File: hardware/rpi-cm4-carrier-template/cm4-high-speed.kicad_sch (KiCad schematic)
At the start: 1 part

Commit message: Added dimensions and updated CM4 component properties to include both receptacle options
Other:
- title: Raspberry Pi Compute Module 4 Shoe Template -> Raspberry Pi Compute Module 4 Carrier Template
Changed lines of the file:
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@@
   (paper "A4")
   (title_block
-    (title "Raspberry Pi Compute Module 4 Shoe Template")
+    (title "Raspberry Pi Compute Module 4 Carrier Template")
     (date "2020-10-31")
     (rev "v01")

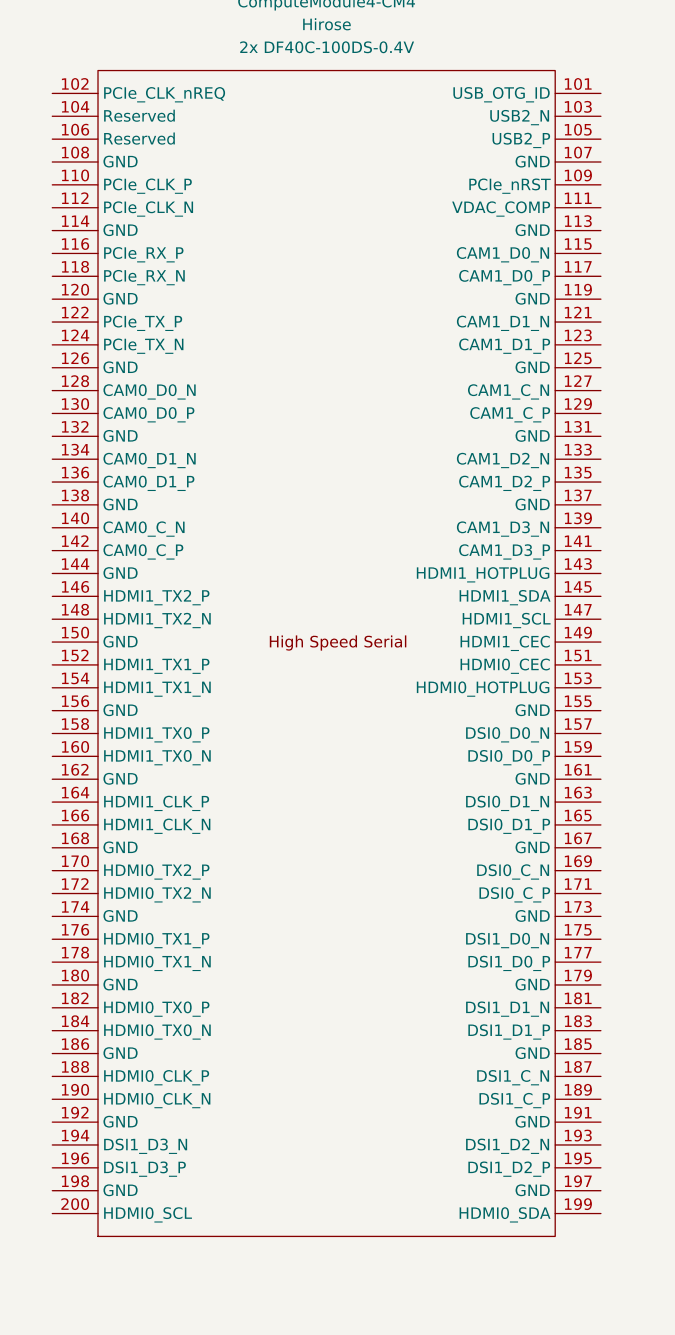
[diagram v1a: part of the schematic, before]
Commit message: Added GND and power lines with labels
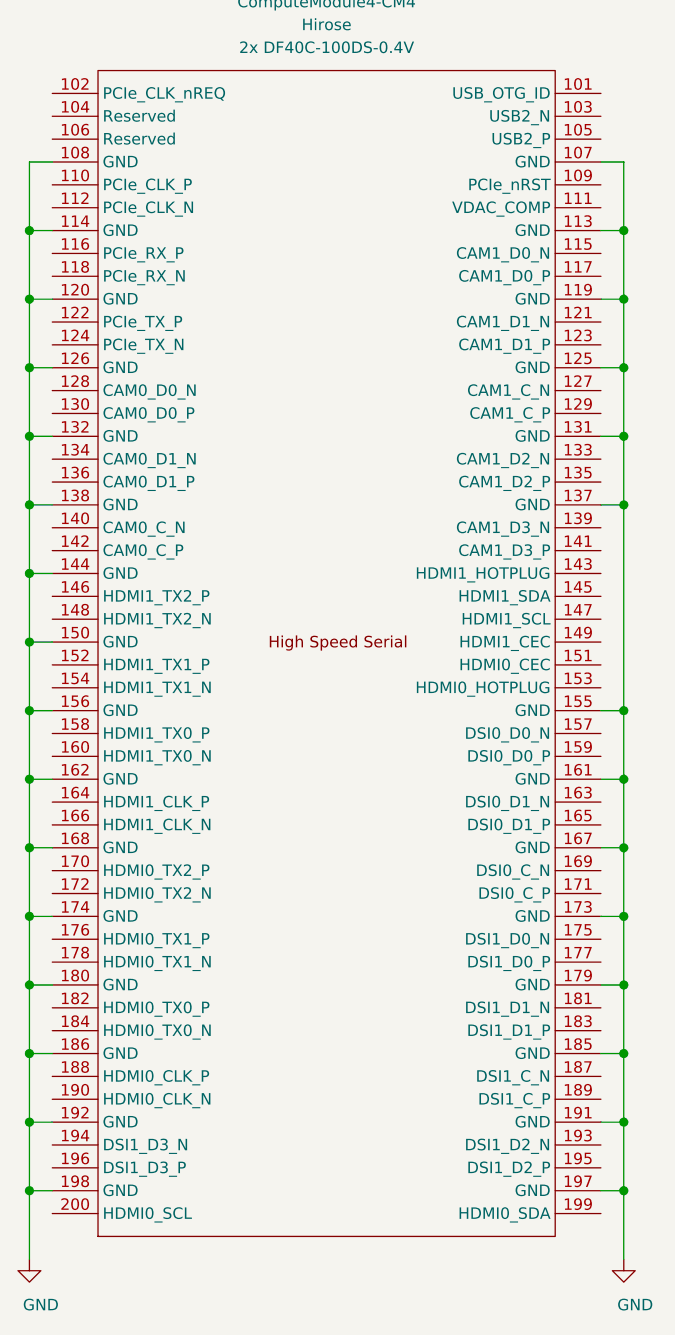
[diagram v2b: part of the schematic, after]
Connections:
- net GND: now reaches Module1.107 (GND)
- net GND: now also Module1.108 (GND), Module1.113 (GND), Module1.114 (GND), Module1.119 (GND), Module1.120 (GND), Module1.125 (GND), Module1.126 (GND), Module1.131 (GND), Module1.132 (GND), Module1.137 (GND), Module1.138 (GND), Module1.144 (GND), Module1.150 (GND), Module1.155 (GND), Module1.156 (GND), Module1.161 (GND), Module1.162 (GND), Module1.167 (GND), Module1.168 (GND), Module1.173 (GND), Module1.174 (GND), Module1.179 (GND), Module1.180 (GND), Module1.185 (GND), Module1.186 (GND), Module1.191 (GND), Module1.192 (GND), Module1.197 (GND), Module1.198 (GND)
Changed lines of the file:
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@@
     (comment 4 "Author: Shawn Hymel")
+  )
+  (junction (at 40.64 60.96) (diameter 1.016) (color 0 0 0 0))
+  (junction (at 40.64 68.58) (diameter 1.016) (color 0 0 0 0))
+  (junction (at 40.64 76.2) (diameter 1.016) (color 0 0 0 0))
+  (junction (at 40.64 83.82) (diameter 1.016) (color 0 0 0 0))
+  (junction (at 40.64 91.44) (diameter 1.016) (color 0 0 0 0))
+  (junction (at 40.64 99.06) (diameter 1.016) (color 0 0 0 0))
+  (junction (at 40.64 106.68) (diameter 1.016) (color 0 0 0 0))
+  (junction (at 40.64 114.3) (diameter 1.016) (color 0 0 0 0))
+  (junction (at 40.64 121.92) (diameter 1.016) (color 0 0 0 0))
+  (junction (at 40.64 129.54) (diameter 1.016) (color 0 0 0 0))
+  (junction (at 40.64 137.16) (diameter 1.016) (color 0 0 0 0))
+  (junction (at 40.64 144.78) (diameter 1.016) (color 0 0 0 0))
+  (junction (at 40.64 152.4) (diameter 1.016) (color 0 0 0 0))
+  (junction (at 40.64 160.02) (diameter 1.016) (color 0 0 0 0))
+  (junction (at 40.64 167.64) (diameter 1.016) (color 0 0 0 0))
+  (junction (at 106.68 60.96) (diameter 1.016) (color 0 0 0 0))
+  (junction (at 106.68 68.58) (diameter 1.016) (color 0 0 0 0))
+  (junction (at 106.68 76.2) (diameter 1.016) (color 0 0 0 0))
+  (junction (at 106.68 83.82) (diameter 1.016) (color 0 0 0 0))
+  (junction (at 106.68 91.44) (diameter 1.016) (color 0 0 0 0))
+  (junction (at 106.68 114.3) (diameter 1.016) (color 0 0 0 0))
+  (junction (at 106.68 121.92) (diameter 1.016) (color 0 0 0 0))
+  (junction (at 106.68 129.54) (diameter 1.016) (color 0 0 0 0))
+  (junction (at 106.68 137.16) (diameter 1.016) (color 0 0 0 0))
+  (junction (at 106.68 144.78) (diameter 1.016) (color 0 0 0 0))
+  (junction (at 106.68 152.4) (diameter 1.016) (color 0 0 0 0))
+  (junction (at 106.68 160.02) (diameter 1.016) (color 0 0 0 0))
+  (junction (at 106.68 167.64) (diameter 1.016) (color 0 0 0 0))
+  (wire (pts (xy 40.64 53.34) (xy 40.64 60.96))
+    (stroke (width 0) (type solid) (color 0 0 0 0))
+  )
+  (wire (pts (xy 40.64 53.34) (xy 43.18 53.34))
+    (stroke (width 0) (type solid) (color 0 0 0 0))
+  )
+  (wire (pts (xy 40.64 60.96) (xy 40.64 68.58))
+    (stroke (width 0) (type solid) (color 0 0 0 0))
+  )
+  (wire (pts (xy 40.64 60.96) (xy 43.18 60.96))
+    (stroke (width 0) (type solid) (color 0 0 0 0))
+  )
+  (wire (pts (xy 40.64 68.58) (xy 40.64 76.2))
+    (stroke (width 0) (type solid) (color 0 0 0 0))
+  )
+  (wire (pts (xy 40.64 68.58) (xy 43.18 68.58))
+    (stroke (width 0) (type solid) (color 0 0 0 0))
+  )
+  (wire (pts (xy 40.64 76.2) (xy 40.64 83.82))
+    (stroke (width 0) (type solid) (color 0 0 0 0))
+  )
+  (wire (pts (xy 40.64 76.2) (xy 43.18 76.2))
+    (stroke (width 0) (type solid) (color 0 0 0 0))
+  )
+  (wire (pts (xy 40.64 83.82) (xy 40.64 91.44))
+    (stroke (width 0) (type solid) (color 0 0 0 0))
+  )
+  (wire (pts (xy 40.64 83.82) (xy 43.18 83.82))
+    (stroke (width 0) (type solid) (color 0 0 0 0))
+  )
+  (wire (pts (xy 40.64 91.44) (xy 40.64 99.06))
+    (stroke (width 0) (type solid) (color 0 0 0 0))
+  )
+  (wire (pts (xy 40.64 91.44) (xy 43.18 91.44))
+    (stroke (width 0) (type solid) (color 0 0 0 0))
+  )
+  (wire (pts (xy 40.64 99.06) (xy 40.64 106.68))
+    (stroke (width 0) (type solid) (color 0 0 0 0))
+  )
+  (wire (pts (xy 40.64 99.06) (xy 43.18 99.06))
+    (stroke (width 0) (type solid) (color 0 0 0 0))
+  )
+  (wire (pts (xy 40.64 106.68) (xy 40.64 114.3))
+    (stroke (width 0) (type solid) (color 0 0 0 0))
+  )
+  (wire (pts (xy 40.64 106.68) (xy 43.18 106.68))
+    (stroke (width 0) (type solid) (color 0 0 0 0))
+  )
+  (wire (pts (xy 40.64 114.3) (xy 40.64 121.92))
+    (stroke (width 0) (type solid) (color 0 0 0 0))
+  )
+  (wire (pts (xy 40.64 114.3) (xy 43.18 114.3))
+    (stroke (width 0) (type solid) (color 0 0 0 0))
+  )
+  (wire (pts (xy 40.64 121.92) (xy 40.64 129.54))
+    (stroke (width 0) (type solid) (color 0 0 0 0))
+  )
+  (wire (pts (xy 40.64 121.92) (xy 43.18 121.92))
+    (stroke (width 0) (type solid) (color 0 0 0 0))
+  )
+  (wire (pts (xy 40.64 129.54) (xy 40.64 137.16))
+    (stroke (width 0) (type solid) (color 0 0 0 0))
+  )
+  (wire (pts (xy 40.64 129.54) (xy 43.18 129.54))
+    (stroke (width 0) (type solid) (color 0 0 0 0))
+  )
+  (wire (pts (xy 40.64 137.16) (xy 40.64 144.78))
+    (stroke (width 0) (type solid) (color 0 0 0 0))
+  )
+  (wire (pts (xy 40.64 137.16) (xy 43.18 137.16))
+    (stroke (width 0) (type solid) (color 0 0 0 0))
+  )
+  (wire (pts (xy 40.64 144.78) (xy 40.64 152.4))
+    (stroke (width 0) (type solid) (color 0 0 0 0))
+  )
+  (wire (pts (xy 40.64 144.78) (xy 43.18 144.78))
+    (stroke (width 0) (type solid) (color 0 0 0 0))
+  )
+  (wire (pts (xy 40.64 152.4) (xy 40.64 160.02))
+    (stroke (width 0) (type solid) (color 0 0 0 0))
+  )
+  (wire (pts (xy 40.64 152.4) (xy 43.18 152.4))
+    (stroke (width 0) (type solid) (color 0 0 0 0))
+  )
+  (wire (pts (xy 40.64 160.02) (xy 40.64 167.64))
+    (stroke (width 0) (type solid) (color 0 0 0 0))
+  )
+  (wire (pts (xy 40.64 160.02) (xy 43.18 160.02))
+    (stroke (width 0) (type solid) (color 0 0 0 0))
+  )
+  (wire (pts (xy 40.64 167.64) (xy 40.64 175.26))
+    (stroke (width 0) (type solid) (color 0 0 0 0))
+  )
+  (wire (pts (xy 40.64 167.64) (xy 43.18 167.64))
+    (stroke (width 0) (type solid) (color 0 0 0 0))
+  )
+  (wire (pts (xy 104.14 53.34) (xy 106.68 53.34))
+    (stroke (width 0) (type solid) (color 0 0 0 0))
+  )
+  (wire (pts (xy 104.14 60.96) (xy 106.68 60.96))
+    (stroke (width 0) (type solid) (color 0 0 0 0))
+  )
+  (wire (pts (xy 104.14 68.58) (xy 106.68 68.58))
+    (stroke (width 0) (type solid) (color 0 0 0 0))
+  )
+  (wire (pts (xy 104.14 76.2) (xy 106.68 76.2))
+    (stroke (width 0) (type solid) (color 0 0 0 0))
+  )
+  (wire (pts (xy 104.14 83.82) (xy 106.68 83.82))
+    (stroke (width 0) (type solid) (color 0 0 0 0))
+  )
+  (wire (pts (xy 104.14 91.44) (xy 106.68 91.44))
+    (stroke (width 0) (type solid) (color 0 0 0 0))
+  )
+  (wire (pts (xy 104.14 114.3) (xy 106.68 114.3))
+    (stroke (width 0) (type solid) (color 0 0 0 0))
+  )
+  (wire (pts (xy 104.14 121.92) (xy 106.68 121.92))
+    (stroke (width 0) (type solid) (color 0 0 0 0))
+  )
+  (wire (pts (xy 104.14 129.54) (xy 106.68 129.54))
+    (stroke (width 0) (type solid) (color 0 0 0 0))
+  )
+  (wire (pts (xy 104.14 137.16) (xy 106.68 137.16))
+    (stroke (width 0) (type solid) (color 0 0 0 0))
+  )
+  (wire (pts (xy 104.14 144.78) (xy 106.68 144.78))
+    (stroke (width 0) (type solid) (color 0 0 0 0))
+  )
+  (wire (pts (xy 104.14 152.4) (xy 106.68 152.4))
+    (stroke (width 0) (type solid) (color 0 0 0 0))
+  )
+  (wire (pts (xy 104.14 160.02) (xy 106.68 160.02))
+    (stroke (width 0) (type solid) (color 0 0 0 0))
+  )
+  (wire (pts (xy 104.14 167.64) (xy 106.68 167.64))
+    (stroke (width 0) (type solid) (color 0 0 0 0))
+  )
+  (wire (pts (xy 106.68 53.34) (xy 106.68 60.96))
+    (stroke (width 0) (type solid) (color 0 0 0 0))
+  )
+  (wire (pts (xy 106.68 60.96) (xy 106.68 68.58))
+    (stroke (width 0) (type solid) (color 0 0 0 0))
+  )
+  (wire (pts (xy 106.68 68.58) (xy 106.68 76.2))
+    (stroke (width 0) (type solid) (color 0 0 0 0))
+  )
+  (wire (pts (xy 106.68 76.2) (xy 106.68 83.82))
+    (stroke (width 0) (type solid) (color 0 0 0 0))
+  )
+  (wire (pts (xy 106.68 83.82) (xy 106.68 91.44))
+    (stroke (width 0) (type solid) (color 0 0 0 0))
+  )
+  (wire (pts (xy 106.68 91.44) (xy 106.68 114.3))
+    (stroke (width 0) (type solid) (color 0 0 0 0))
+  )
+  (wire (pts (xy 106.68 114.3) (xy 106.68 121.92))
+    (stroke (width 0) (type solid) (color 0 0 0 0))
+  )
+  (wire (pts (xy 106.68 121.92) (xy 106.68 129.54))
+    (stroke (width 0) (type solid) (color 0 0 0 0))
+  )
+  (wire (pts (xy 106.68 129.54) (xy 106.68 137.16))
+    (stroke (width 0) (type solid) (color 0 0 0 0))
+  )
+  (wire (pts (xy 106.68 137.16) (xy 106.68 144.78))
+    (stroke (width 0) (type solid) (color 0 0 0 0))
+  )
+  (wire (pts (xy 106.68 144.78) (xy 106.68 152.4))
+    (stroke (width 0) (type solid) (color 0 0 0 0))
+  )
+  (wire (pts (xy 106.68 152.4) (xy 106.68 160.02))
+    (stroke (width 0) (type solid) (color 0 0 0 0))
+  )
+  (wire (pts (xy 106.68 160.02) (xy 106.68 167.64))
+    (stroke (width 0) (type solid) (color 0 0 0 0))
+  )
+  (wire (pts (xy 106.68 167.64) (xy 106.68 175.26))
+    (stroke (width 0) (type solid) (color 0 0 0 0))
+  )
+  (symbol (lib_id "power:GND") (at 40.64 175.26 0) (unit 1)
+    (in_bom yes) (on_board yes)
+    (property "Reference" "#PWR?" (id 0) (at 40.64 181.61 0)
+      (effects (font (size 1.27 1.27)) hide)
+    )
+    (property "Value" "GND" (id 1) (at 41.91 180.34 0))
+    (property "Footprint" "" (id 2) (at 40.64 175.26 0)
+      (effects (font (size 1.27 1.27)) hide)
+    )
+    (property "Datasheet" "" (id 3) (at 40.64 175.26 0)
+      (effects (font (size 1.27 1.27)) hide)
+    )
+  )
+  (symbol (lib_id "power:GND") (at 106.68 175.26 0) (unit 1)
+    (in_bom yes) (on_board yes)
+    (property "Reference" "#PWR?" (id 0) (at 106.68 181.61 0)
+      (effects (font (size 1.27 1.27)) hide)
+    )
+    (property "Value" "GND" (id 1) (at 107.95 180.34 0))
+    (property "Footprint" "" (id 2) (at 106.68 175.26 0)
+      (effects (font (size 1.27 1.27)) hide)
+    )
+    (property "Datasheet" "" (id 3) (at 106.68 175.26 0)
+      (effects (font (size 1.27 1.27)) hide)
+    )
   )
   (symbol (lib_id "CM4IO:ComputeModule4-CM4") (at -66.04 106.68 0) (unit 2)

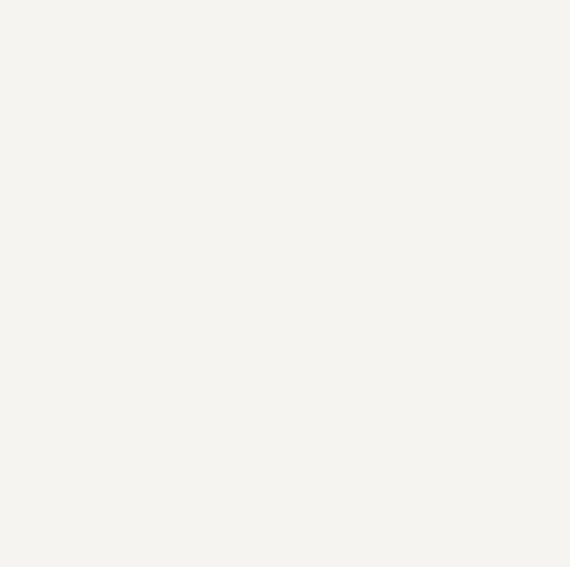
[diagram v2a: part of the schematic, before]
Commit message: Moved libraries to separate folders
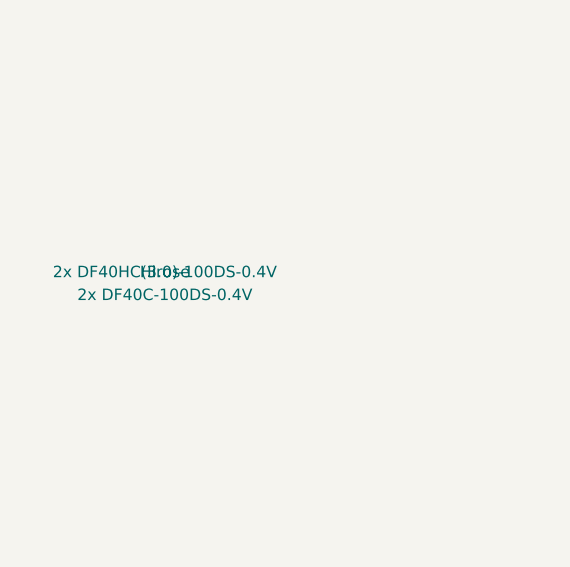
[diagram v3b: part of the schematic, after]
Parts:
- Module1: MPN (none) -> 2x DF40C-100DS-0.4V; MPN (Alt) (none) -> 2x DF40HC(3.0)-100DS-0.4V; Manufacturer (none) -> Hirose
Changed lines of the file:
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@@
       (effects (font (size 1.27 1.27)) hide)
     )
+    (property "Manufacturer" "Hirose" (id 8) (at -66.04 106.68 0))
+    (property "MPN" "2x DF40C-100DS-0.4V" (id 9) (at -66.04 109.22 0))
+    (property "MPN (Alt)" "2x DF40HC(3.0)-100DS-0.4V" (id 10) (at -66.04 106.68 0))
   )
 )
